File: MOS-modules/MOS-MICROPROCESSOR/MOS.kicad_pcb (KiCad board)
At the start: 2 copper layers, 61 x 96.5 mm, 12 parts, among them J1 Conn_01x03_Male, J2 Conn_01x34_Male, U1 6502, X1 CXO_DIP8

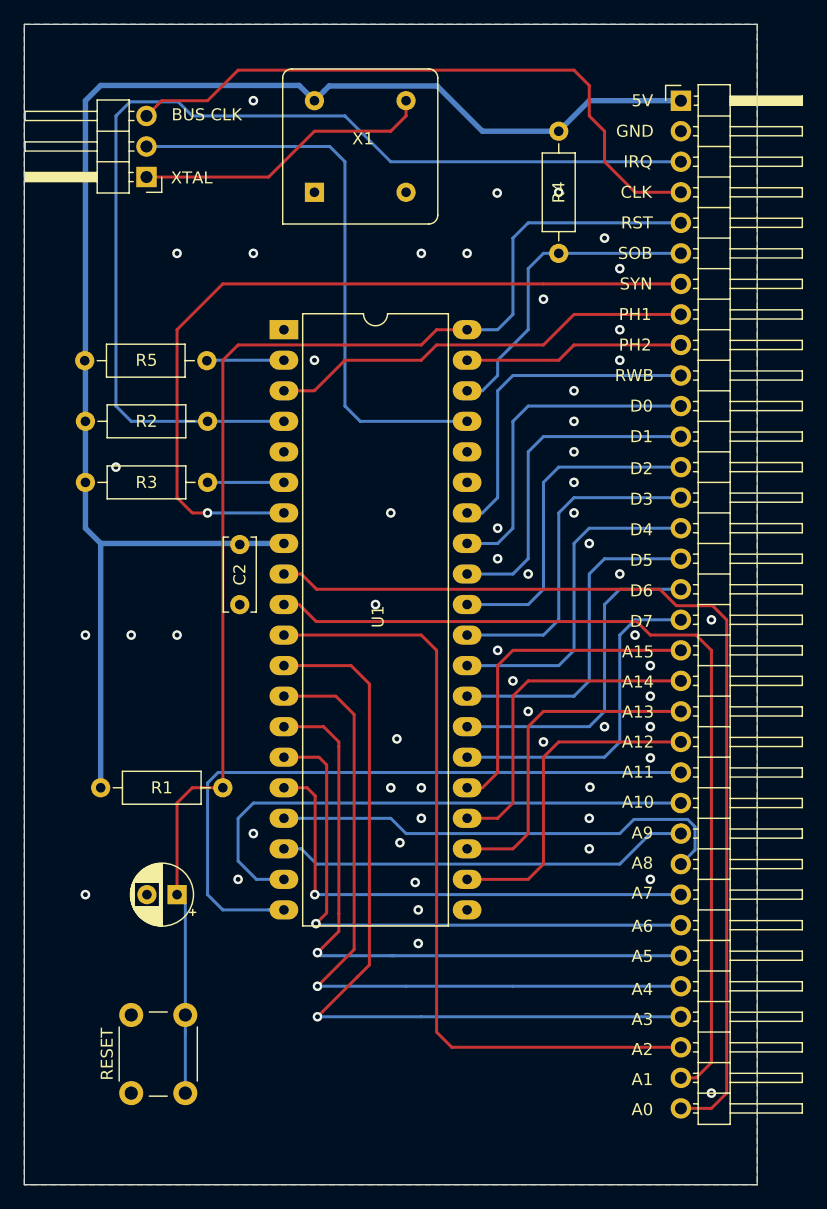
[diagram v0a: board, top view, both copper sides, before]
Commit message: MOS 6503 Rev B
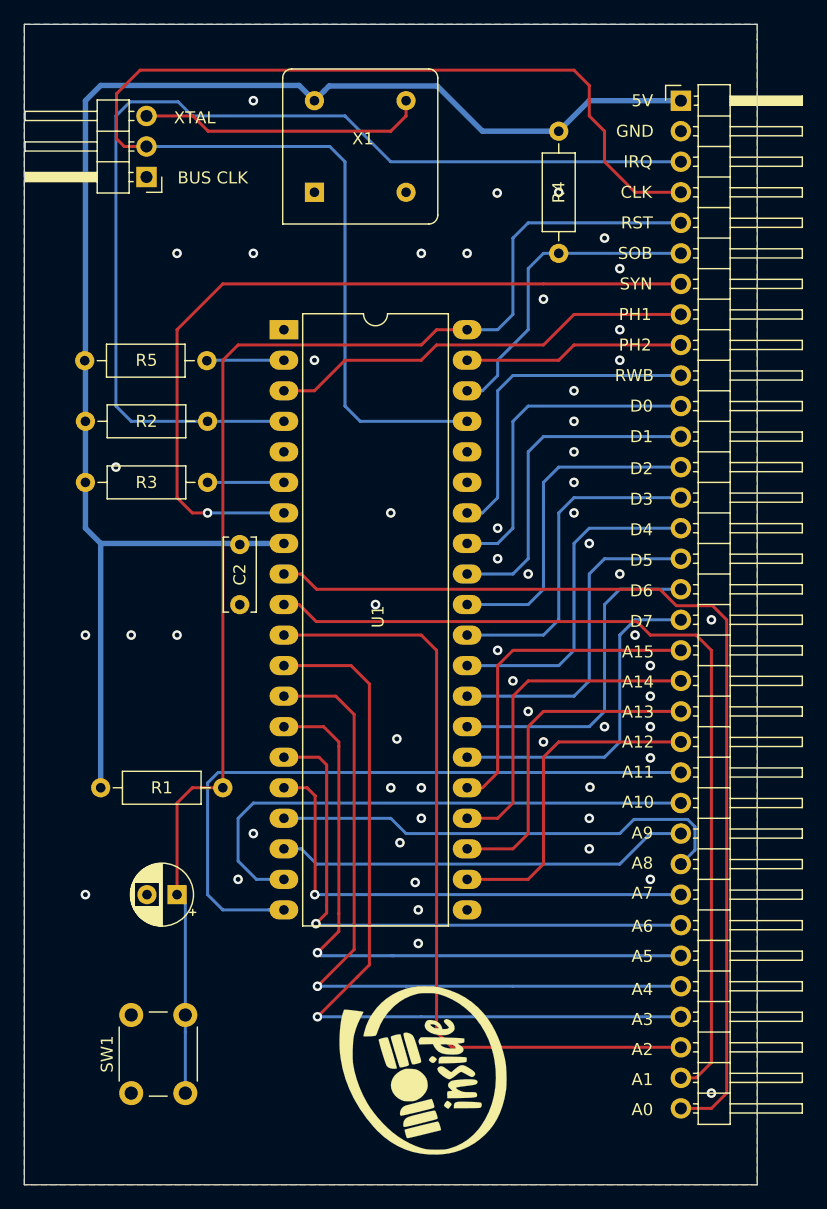
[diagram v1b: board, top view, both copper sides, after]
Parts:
- added G***: LOGO, logos:logo_mosinside_bueno, F.Cu at (133.5, 149.2)
- added REF**: KiCad-Logo2_5mm_SilkScreen, Symbol:KiCad-Logo2_5mm_SilkScreen, B.Cu at (145.0, 106.5)
- renumbered RESET to SW1
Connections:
- J1 pad 1: /CLK_INTERNAL -> (no net)
- J1 pad 2: /CLK_INPUT -> /CLK
- J1 pad 3: /CLK -> /CLK_INTERNAL
- U1 pad 37: /CLK_INPUT -> /CLK
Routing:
- net /CLK: track 53.2 -> 109.5 mm
- net /CLK_INPUT: track 48.0 -> 0.00 mm
- net /CLK_INTERNAL: track 25.0 -> 23.9 mm
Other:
- board text added: "Elppa - based on Ben Eater’s MOS 6502 Designed by Jordi Gauchía & Pepe Chorva in the sunny Mediterranean Coast MOS module - Rev B 09/2020"
- board text added: "S/N:"
- board text removed: "Elppa - based on Ben Eater’s MOS 6502 Designed by Jordi Gauchía & Pepe Chorva in the sunny Mediterranean Coast MOS module - Rev A 08/2020"
- board text removed: "Serial Number:"
